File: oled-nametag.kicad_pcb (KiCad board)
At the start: 4 copper layers, 88 x 30 mm, 104 parts, among them J1 USB_C_Receptacle_USB2.0, Q1 AO3401A, Q2 AO3401A, Q3 FS8205A, Q6 2N7002, SW1 Power, SW2 BTN1, SW3 BTN2, SW4 BTN3, U10 BQ27546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

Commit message: wip
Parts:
- added C26: 10uF, Capacitor_SMD:C_0402_1005Metric, F.Cu at (45.0, 25.6)
- moved C25 27.1 mm to (94.7, 38.6)
- moved Q3 27.1 mm to (97.8, 38.5)
- moved R12 27.1 mm to (94.7, 36.3)
- moved R13 27.1 mm to (100.7, 35.9)
- moved U7 27.1 mm to (97.8, 35.0)
- moved C36 14.8 mm to (85.2, 31.1)
- moved C38 14.8 mm to (87.0, 31.1)
- moved R24 14.8 mm to (85.6, 29.6)
- moved R25 14.8 mm to (84.6, 29.6)
- moved R26 14.8 mm to (85.1, 27.6)
- moved C29 14.8 mm to (83.3, 33.1)
- moved C34 14.8 mm to (83.3, 34.1)
- moved C35 14.8 mm to (85.0, 35.1)
- moved R22 14.8 mm to (83.6, 35.6)
- moved R23 14.8 mm to (85.5, 36.6)
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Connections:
- R1 pad 1: VBUS -> +3V3
- U3 pad 43: unconnected-(U3-GPIO38-Pad43) -> /ESP32/PWR_EN
- U3 pad 9: /ESP32/PWR_EN -> unconnected-(U3-GPIO4-Pad9)
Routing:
- net Net-(D3-K): track 0.00 -> 136.2 mm, vias 0 -> 9
- net GND: track 0.00 -> 57.2 mm, vias 0 -> 40
- net Net-(D3-A): track 0.00 -> 41.6 mm, vias 0 -> 2
- net /Power/VUSB: track 0.00 -> 35.3 mm
- net +3V3: track 0.00 -> 30.7 mm, vias 0 -> 12
- net VCC: track 0.00 -> 22.5 mm, vias 0 -> 2
- net Net-(U1-BS0): track 0.00 -> 14.0 mm, vias 0 -> 2
- net Net-(U1-IREF): track 0.00 -> 11.7 mm, vias 0 -> 2
- net Net-(D1-A): track 0.00 -> 9.85 mm, vias 0 -> 2
- net Net-(J1-CC2): track 0.00 -> 9.34 mm
- net Net-(U3-XTAL_P): track 0.00 -> 7.97 mm
- net /ESP32/PWR_EN: track 0.00 -> 7.96 mm
- net /ESP32/~{RST}: track 0.00 -> 7.09 mm
- net Net-(U1-VCOMH): track 0.00 -> 6.80 mm
- net Net-(J1-CC1): track 0.00 -> 6.54 mm
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
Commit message: Finish ESP32 fanout
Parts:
- added C32: 10uF, Capacitor_SMD:C_0402_1005Metric, F.Cu at (50.5, 26.1)
- added R16: 5.1k, Resistor_SMD:R_0402_1005Metric, F.Cu at (44.7, 27.2)
- added R31: 5.1k, Resistor_SMD:R_0402_1005Metric, F.Cu at (37.2, 21.3)
- moved C23 54.4 mm to (145.8, 22.9)
- moved C25 54.4 mm to (149.1, 37.6)
- moved C27 54.4 mm to (147.7, 22.9)
- moved C29 54.4 mm to (137.7, 32.1)
- moved C36 54.4 mm to (139.6, 30.1)
- moved Q3 54.4 mm to (152.1, 37.5)
- moved R12 54.4 mm to (149.1, 35.3)
- moved R13 54.4 mm to (155.1, 34.9)
- moved R14 54.4 mm to (147.7, 27.9)
- moved U7 54.4 mm to (152.1, 34.0)
- moved C34 54.4 mm to (137.6, 33.1)
- moved C35 54.4 mm to (139.3, 34.1)
- moved C37 54.4 mm to (137.8, 30.1)
- moved C38 54.4 mm to (141.3, 30.1)
- moved R15 54.4 mm to (149.8, 24.6)
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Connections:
- C23 pad 1: /Power/VUSB -> VBUS
- C33 pad 1: /Power/VUSB -> VBUS
- FB1 pad 1: /Power/VUSB -> VBUS
- J1 pad A4: /Power/VUSB -> VBUS
- J1 pad A9: /Power/VUSB -> VBUS
- J1 pad B4: /Power/VUSB -> VBUS
- J1 pad B9: /Power/VUSB -> VBUS
- R28 pad 2: /Power/VUSB -> VBUS
- U3 pad 10: /ESP32/PDM_CLK -> /ESP32/~{BTN3}
- U3 pad 11: /ESP32/PDM_DATA -> /ESP32/~{BTN2}
- U3 pad 12: /ESP32/OLED_RST -> unconnected-(U3-GPIO7-Pad12)
- U3 pad 13: /ESP32/OLED_CS -> unconnected-(U3-GPIO8-Pad13)
- U3 pad 14: /ESP32/OLED_DC -> unconnected-(U3-GPIO9-Pad14)
- U3 pad 15: /ESP32/OLED_CLK -> unconnected-(U3-GPIO10-Pad15)
- U3 pad 16: /ESP32/OLED_DATA -> unconnected-(U3-GPIO11-Pad16)
- U3 pad 17: /ESP32/OLED_EN -> /ESP32/~{BTN1}
- U3 pad 18: /ESP32/~{CHRG} -> unconnected-(U3-GPIO13-Pad18)
- U3 pad 19: /ESP32/~{STAT2} -> /ESP32/OLED_EN
- U3 pad 24: /ESP32/~{BTN1} -> /ESP32/OLED_CS
- U3 pad 27: /ESP32/~{BTN2} -> /ESP32/OLED_RST
- U3 pad 38: /ESP32/~{BTN3} -> /ESP32/OLED_CLK
- U3 pad 39: /ESP32/USB_DET -> /ESP32/OLED_DC
- U3 pad 40: unconnected-(U3-GPIO35-Pad40) -> /ESP32/PWR_EN
- U3 pad 41: unconnected-(U3-GPIO36-Pad41) -> /ESP32/OLED_DATA
- U3 pad 42: unconnected-(U3-GPIO37-Pad42) -> /ESP32/PDM_DATA
- U3 pad 43: /ESP32/PWR_EN -> /ESP32/PDM_CLK
- U3 pad 5: unconnected-(U3-GPIO0-Pad5) -> Net-(U3-GPIO0)
- U3 pad 51: unconnected-(U3-GPIO45-Pad51) -> Net-(U3-GPIO45)
- U3 pad 52: unconnected-(U3-GPIO46-Pad52) -> /ESP32/~{STAT2}
- U3 pad 6: unconnected-(U3-GPIO1-Pad6) -> /ESP32/~{CHRG}
- U3 pad 9: unconnected-(U3-GPIO4-Pad9) -> /ESP32/USB_DET
- U8 pad 1: /Power/VUSB -> VBUS
- U8 pad 8: /Power/VUSB -> VBUS
- U9 pad 5: +5V -> VBUS
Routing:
- net /ESP32/~{BTN2}: track 0.00 -> 60.8 mm, vias 0 -> 3
- net /ESP32/D-: track 0.00 -> 52.7 mm, vias 0 -> 4
- net /ESP32/D+: track 0.00 -> 51.2 mm, vias 0 -> 4
- net /ESP32/~{BTN3}: track 0.00 -> 49.9 mm, vias 0 -> 4
- net /ESP32/USB_DET: track 0.00 -> 47.6 mm, vias 0 -> 2
- net /ESP32/~{CHRG}: track 0.00 -> 42.5 mm, vias 0 -> 2
- net VCC: track 22.5 -> 64.4 mm, vias 2 -> 4
- net /ESP32/SCL: track 0.00 -> 41.6 mm, vias 0 -> 3
- net /ESP32/~{STAT2}: track 0.00 -> 41.1 mm, vias 0 -> 2
- net VBUS: track 0.00 -> 35.9 mm, vias 0 -> 1
- net /Power/VUSB: track 35.3 -> 0.00 mm
- net GND: track 57.2 -> 92.2 mm, vias 40 -> 53
- net /ESP32/PWR_ON: track 0.00 -> 33.6 mm, vias 0 -> 4
- net Net-(Q2-D): track 0.00 -> 33.2 mm, vias 0 -> 2
- net /ESP32/OLED_CLK: track 0.00 -> 30.7 mm, vias 0 -> 2
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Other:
- outline, holes or cut-outs redrawn

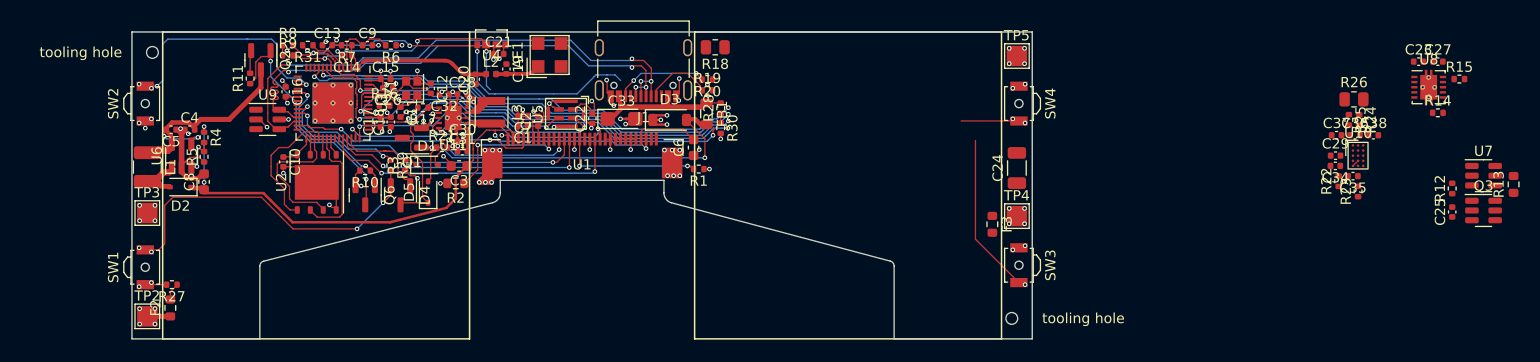
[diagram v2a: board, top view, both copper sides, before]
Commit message: Add power planes
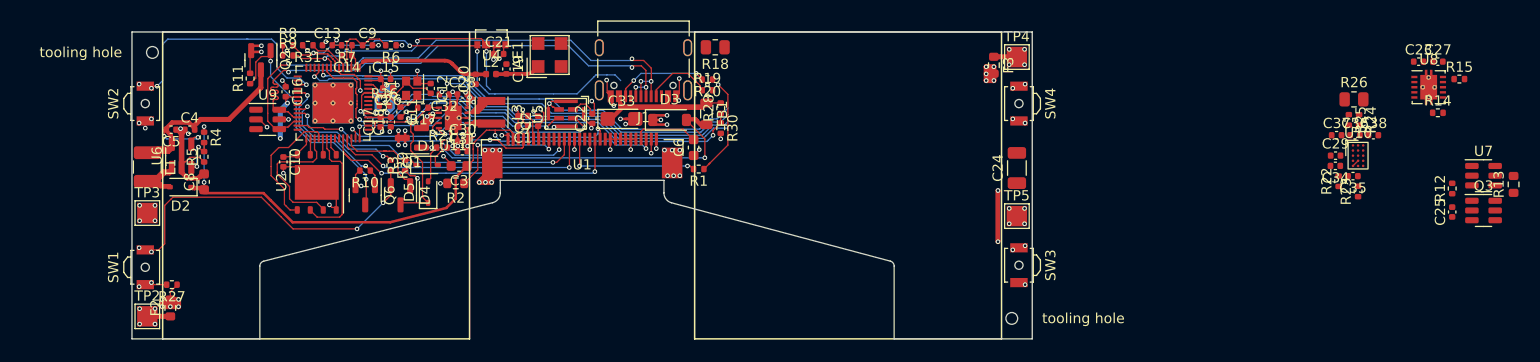
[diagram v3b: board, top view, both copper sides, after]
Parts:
- moved TP5 15.6 mm to (106.5, 38.0)
- moved F3 15.6 mm to (104.2, 23.2)
- moved TP4 15.6 mm to (106.5, 22.4)
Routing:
- net Net-(D3-K): track 148.3 -> 194.2 mm, vias 10 -> 12
- net +3V3: track 34.9 -> 55.1 mm, vias 15 -> 18
- net +BATT: track 1.67 -> 18.9 mm, vias 0 -> 14
- net /ESP32/~{BTN2}: track 60.8 -> 44.8 mm, vias 3 -> 2
- net GND: track 92.2 -> 100.4 mm, vias 53 -> 56
- net /ESP32/~{BTN3}: track 49.9 -> 45.1 mm, vias 4 -> 3
- net Net-(F3-Pad1): track 0.00 -> 2.26 mm
- net /ESP32/~{CHRG}: track 42.5 -> 43.0 mm
- net /ESP32/~{STAT2}: track 41.1 -> 41.7 mm, vias 2 -> 1
- added copper zone on In2.Cu, net +3V3
- added copper zone on In2.Cu, net +BATT
- added copper zone on In1.Cu, net GND
- added copper zone on In1.Cu, net GND1

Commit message: Finish first layout revision
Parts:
- added C39: 100nF, Capacitor_SMD:C_0402_1005Metric, F.Cu at (58.4, 26.9)
- added R32: 100R, Resistor_SMD:R_0402_1005Metric, F.Cu at (85.1, 36.3)
- R1: value 5.1k -> 100R
- R13: footprint Resistor_SMD:R_0603_1608Metric -> Resistor_SMD:R_0402_1005Metric
- U10: footprint Package_DSBGA:DSBGA-15_1.95x2.6mm_P0.5mm -> Package_DSBGA:DSBGA-15_BQ27546_1.95x2.6mm_P0.5mm
- moved Q3 56.7 mm to (95.5, 34.4)
- moved R15 55.4 mm to (94.4, 27.2), turned to -90 degrees
- moved C27 54.9 mm to (92.8, 25.5)
- moved U8 54.9 mm to (91.9, 28.0)
- moved C23 54.9 mm to (91.0, 25.5)
- moved R13 54.5 mm to (100.6, 32.1), turned to 180 degrees
- moved R23 54.0 mm to (85.8, 34.7), turned to 0 degrees
- moved R14 53.3 mm to (94.4, 29.1), turned to -90 degrees
- moved U10 52.7 mm to (87.3, 36.8), turned to 180 degrees
- moved U7 52.5 mm to (99.6, 34.4)
- moved C35 51.7 mm to (87.7, 34.7), turned to 0 degrees
- moved C38 50.6 mm to (91.1, 35.9), turned to 90 degrees
- moved R12 50.4 mm to (98.7, 32.1), turned to 0 degrees
- moved C36 49.1 mm to (91.1, 37.8), turned to 90 degrees
- moved R22 48.8 mm to (89.2, 35.0), turned to -90 degrees
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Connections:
- C34 pad 1: Net-(U10-CE) -> Net-(U10-REGIN)
- R22 pad 2: Net-(U10-CE) -> Net-(U10-REGIN)
- U10 pad A2: Net-(U10-SRN) -> unconnected-(U10-HDQ-PadA2)
- U10 pad B1: (no net) -> Net-(U10-SRN)
- U10 pad D2: Net-(U10-CE) -> /Power/DSG
- U10 pad E1: Net-(U10-CE) -> Net-(U10-REGIN)
- U8 pad 8: VBUS -> GND
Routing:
- net +BATT: track 18.9 -> 135.1 mm, vias 14 -> 22
- net VBUS: track 35.9 -> 124.7 mm, vias 1 -> 12
- net Net-(J1-SHIELD): track 0.00 -> 56.9 mm, vias 0 -> 2
- net GND: track 100.4 -> 148.2 mm, vias 56 -> 86
- net /ESP32/~{BTN2}: track 44.8 -> 87.1 mm, vias 2 -> 5
- net /ESP32/SDA: track 26.3 -> 68.2 mm, vias 3 -> 4
- net /ESP32/SCL: track 41.6 -> 70.3 mm, vias 3 -> 4
- net /ESP32/~{BTN3}: track 45.1 -> 72.5 mm, vias 3 -> 4
- net Net-(U7-VSS): track 0.00 -> 20.0 mm
- net Net-(U7-DO): track 0.00 -> 16.0 mm, vias 0 -> 2
- net /ESP32/~{STAT2}: track 41.7 -> 56.0 mm, vias 1 -> 2
- net /ESP32/~{CHRG}: track 43.0 -> 56.7 mm
- net GND1: track 0.00 -> 13.7 mm, vias 8 -> 19
- net (no net): track 7.77 -> 0.00 mm, vias 12 -> 0
- net Net-(U7-CO): track 0.00 -> 6.23 mm, vias 0 -> 2
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
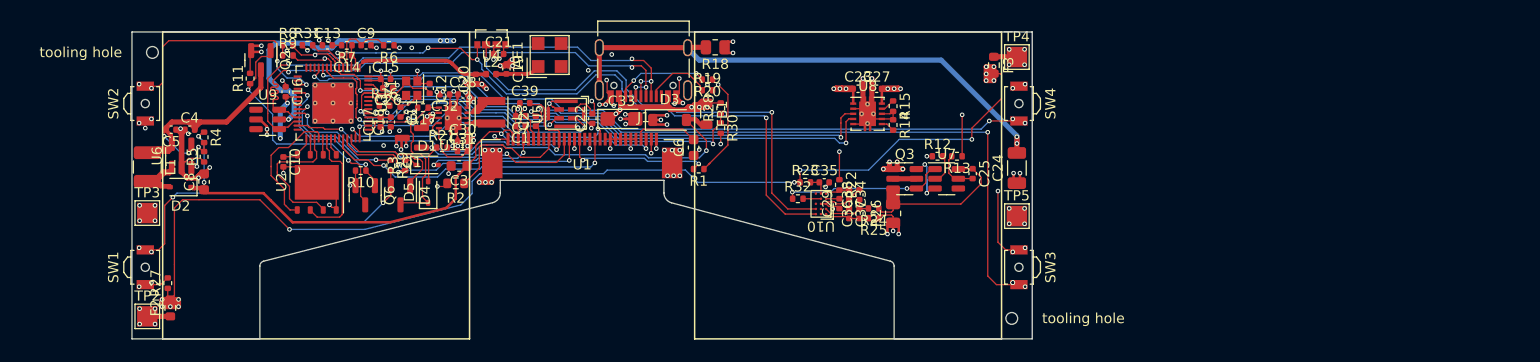
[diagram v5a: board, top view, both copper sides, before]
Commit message: Add 3D models
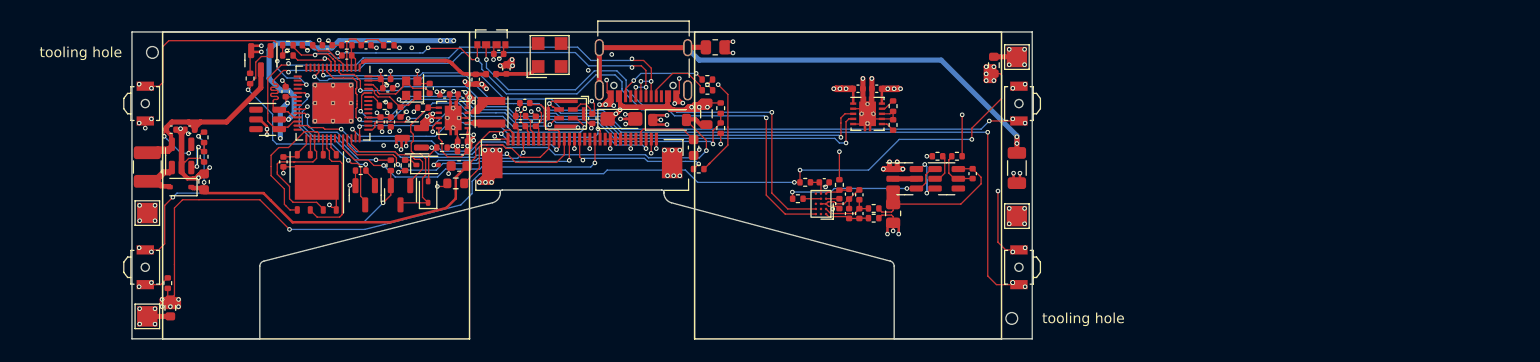
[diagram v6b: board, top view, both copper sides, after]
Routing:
- net GND: track 148.2 -> 153.0 mm
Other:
- outline, holes or cut-outs redrawn

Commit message: Make DRC happy (for the most part)
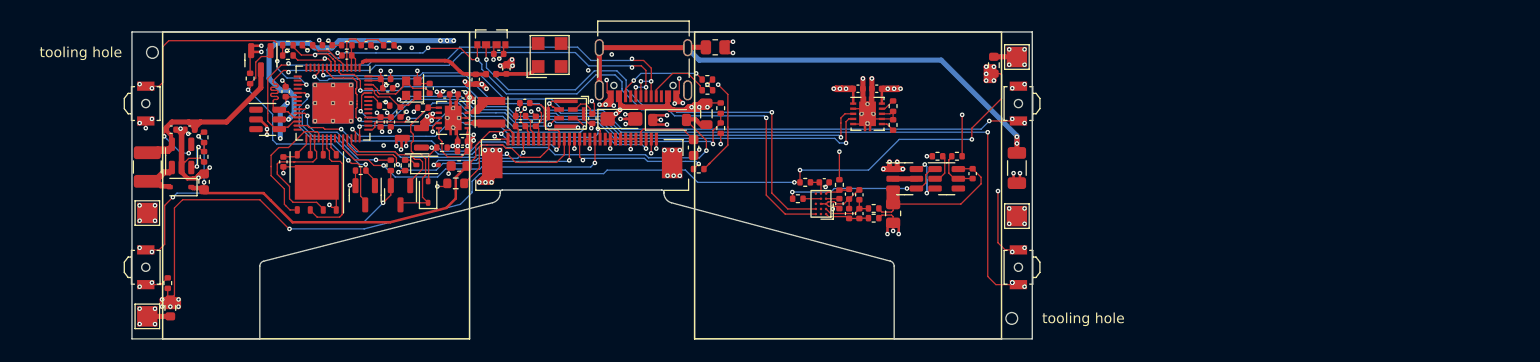
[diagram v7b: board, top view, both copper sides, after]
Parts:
- moved SW1 0.05 mm to (21.4, 43.0)
- moved SW2 0.05 mm to (21.4, 27.0)
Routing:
- net Net-(D3-K): track 193.0 -> 210.8 mm

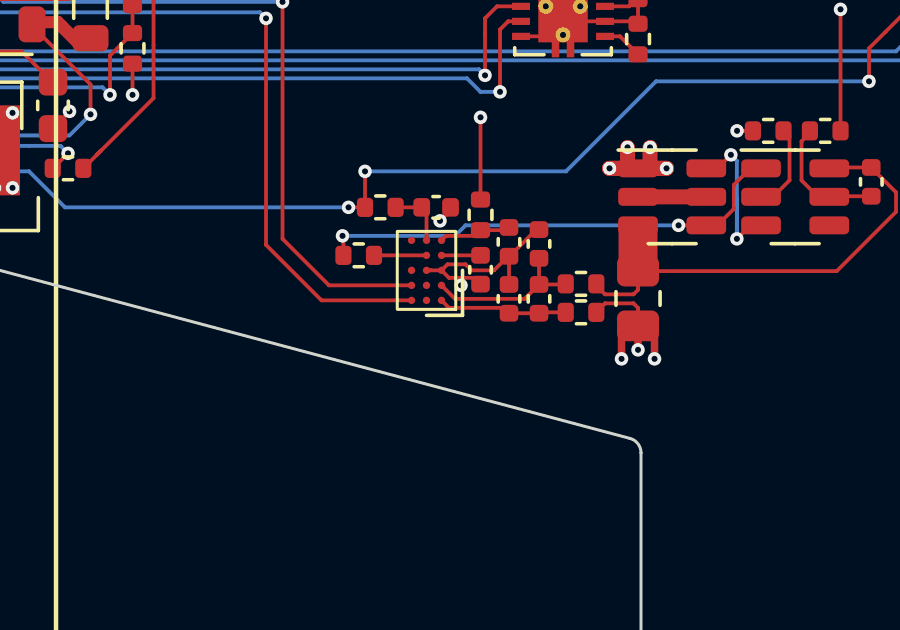
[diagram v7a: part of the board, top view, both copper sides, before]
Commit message: Add fuel gauge thermistor
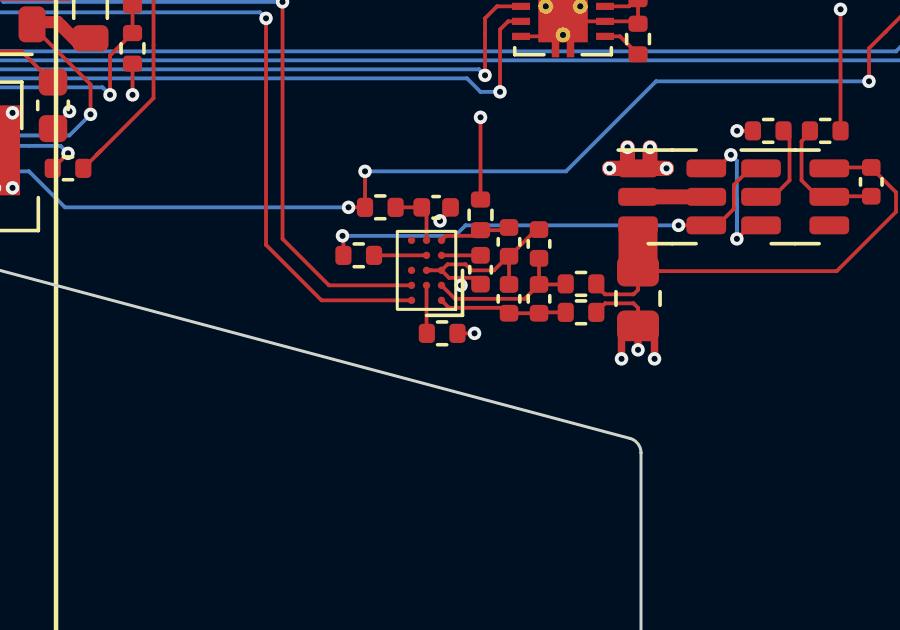
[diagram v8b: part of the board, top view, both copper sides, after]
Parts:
- added R33: 10k, Resistor_SMD:R_0402_1005Metric, F.Cu at (87.9, 38.9)
- U10: footprint Package_DSBGA:DSBGA-15_BQ27546_1.95x2.6mm_P0.5mm -> Package_DSBGA:DSBGA-15_BQ27546_I2C_1.95x2.6mm_P0.5mm
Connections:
- U10 pad B2: unconnected-(U10-TS-PadB2) -> Net-(U10-TS)
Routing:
- net Net-(U10-TS): track 0.00 -> 1.65 mm
- net GND: track 153.0 -> 153.6 mm, vias 86 -> 87
